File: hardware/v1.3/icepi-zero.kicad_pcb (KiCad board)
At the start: 4 copper layers, 65 x 30 mm, 159 parts, among them IC1 IS42S16160J-6BLI, J1 Conn_02x20_Counter_Clockwise, J2 GPDI_C_1.3, J3 USB_C_Receptacle_USB2.0_14P, J4 USB_C_Receptacle_USB2.0_14P, J5 USB_C_Receptacle_USB2.0_14P, J6 Micro_SD_Card_Det2, SW1 SW_Push, SW2 SW_Push, U1 ECP5-CABGA256, U10 TPD2EUSB30A, U12 W25Q128JVS, U2 TLV62569DBV, U3 TLV62569DBV, U4 TLV62569DBV, U5 TPD2EUSB30A, U6 PCA9306DC1, U7 TPD2EUSB30A, U8 TPD2EUSB30A, U9 FT231XQ, Y1 SG-8018CG 50.000000MHz

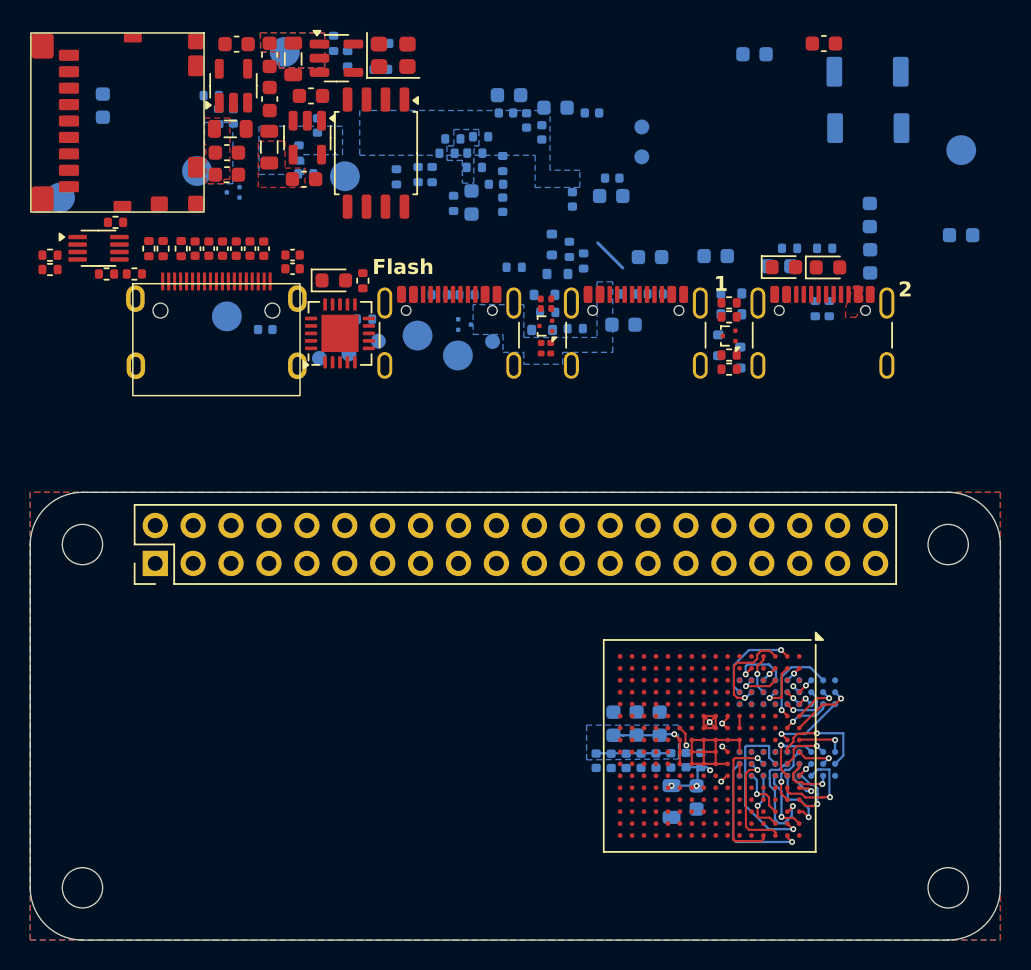
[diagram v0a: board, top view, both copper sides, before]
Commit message: 2.5V LDO
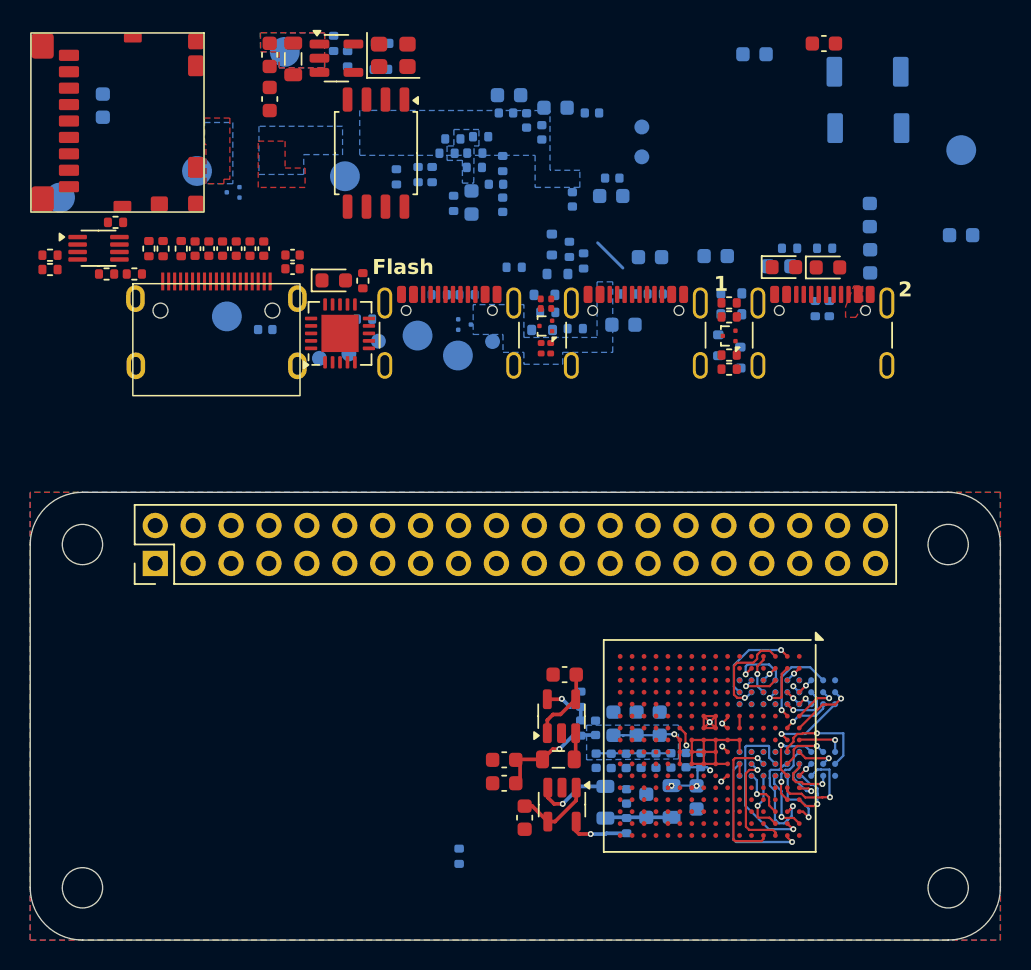
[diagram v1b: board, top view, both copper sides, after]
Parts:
- C19, L2: moved to B.Cu
- moved C18 50.4 mm to (149.1, 149.1), turned to -90 degrees
- moved R8 50.1 mm to (155.9, 149.7)
- moved C20 49.5 mm to (155.9, 147.7)
- moved L2 49.3 mm to (154.5, 148.1)
- moved C19 47.8 mm to (157.2, 148.3), turned to 90 degrees
- moved U3 47.8 mm to (151.6, 148.2)
- moved C11 47.6 mm to (151.7, 139.5)
- moved L1 47.6 mm to (151.3, 145.2)
- moved U2 47.6 mm to (151.5, 142.3)
- moved C14 47.6 mm to (153.8, 143.1)
- moved R6 47.6 mm to (152.8, 143.1)
- moved R7 47.4 mm to (152.8, 141.2), turned to 90 degrees
- moved R9 46.9 mm to (144.7, 151.7), turned to 90 degrees
- moved C13 44.8 mm to (147.7, 146.8), turned to 180 degrees
- moved C12 44.7 mm to (147.7, 145.2), turned to 180 degrees
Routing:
- net +5V: track 49.1 -> 59.4 mm
- net +1V1: track 43.7 -> 50.9 mm, vias 3 -> 4
- net Net-(U3-SW): track 0.00 -> 5.18 mm, vias 0 -> 1
- net +2V5: track 0.00 -> 4.45 mm
- net Net-(U3-FB): track 0.00 -> 4.12 mm, vias 0 -> 1
- net Net-(U2-FB): track 0.00 -> 3.36 mm, vias 0 -> 1
- net Net-(U2-SW): track 0.00 -> 1.80 mm
